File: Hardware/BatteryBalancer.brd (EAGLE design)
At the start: 93.6 x 20.1 mm, 94 parts, among them IC1 OP-AMP, J2 ISP, U1 TAP_POINT, U10 MCP1755, U11 AD7280A, U12 ATMEGA328P_TQFP, U13 CH340C, U2 TAP_POINT, U3 TAP_POINT, U4 TAP_POINT, U5 TAP_POINT, Y1 16MHz

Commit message: Panelized + cammed
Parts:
- added U$8: (no value), echoic#JPG:ECHOIC#JPG
- added U$9: (no value), tech#JPG:TECH#JPG
- moved R34 126.8 mm to (30.4, 2.67), turned to 135 degrees
- moved R10 123.6 mm to (28.3, 2.54), turned to 315 degrees
- moved C2 31.4 mm to (72.4, 2.40)
- moved C1 31.3 mm to (81.9, 2.26)
- moved C12 30.5 mm to (59.2, 16.4)
- moved C19 30.5 mm to (8.38, 3.81)
- moved C3 30.5 mm to (72.5, 6.10)
- moved C4 30.5 mm to (72.5, 9.40)
- moved C5 30.5 mm to (72.5, 12.7)
- moved C6 30.5 mm to (72.5, 16.0)
- moved D3 30.5 mm to (50.3, 3.43)
- moved D5 30.5 mm to (79.4, 19.1)
- moved D6 30.5 mm to (54.6, 19.1)
- moved D7 30.5 mm to (29.8, 19.1)
- moved J1 30.5 mm to (4.19, 6.48)
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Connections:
- net RESET renamed !RESET
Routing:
- net CHARGE: track 21.1 -> 39.7 mm, vias 3 -> 4
- net N$40: track 31.6 -> 25.6 mm
- net GND: track 24.5 -> 26.8 mm, vias 89 -> 86
- net V_RAW: track 47.1 -> 45.8 mm
- net !RESET: track 90.1 -> 89.6 mm, vias 5 -> 4
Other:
- board size 93.6 x 20.1 mm -> 93.3 x 20.3 mm

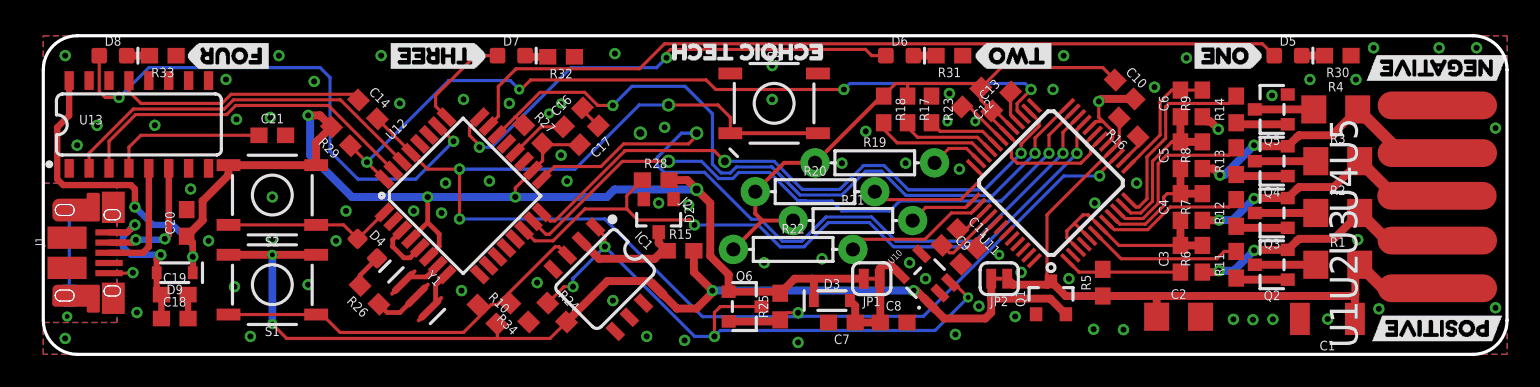
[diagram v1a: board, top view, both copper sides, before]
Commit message: Increase manufacturability, re panelize + CAM
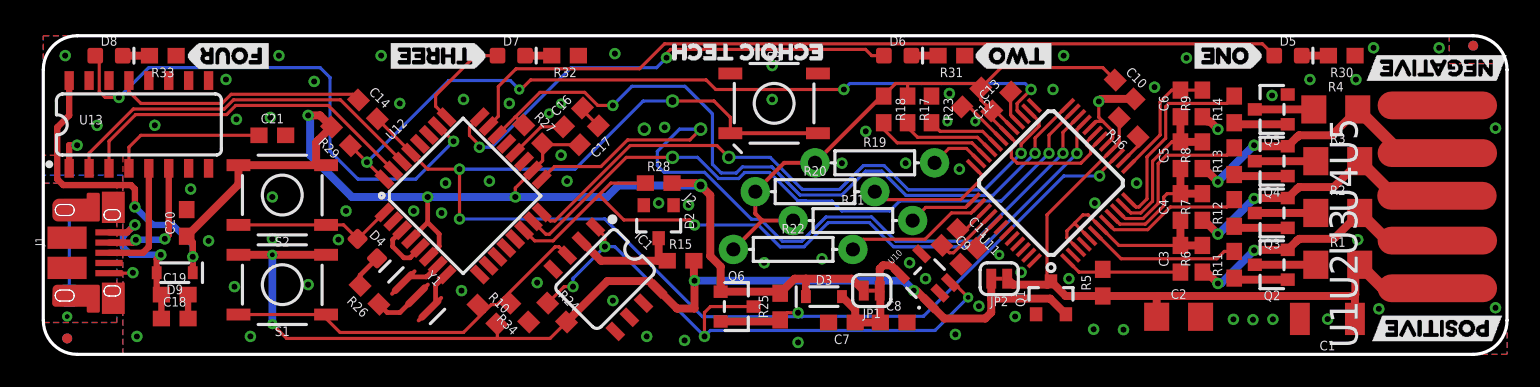
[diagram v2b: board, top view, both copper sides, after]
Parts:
- added FD1, FD2, FD3, FD4: FIDUCIALUFIDUCIAL, SparkFun-Aesthetics:FIDUCIAL-MICRO
- moved FRAME1 83.7 mm to (11.4, -12.1)
- moved JP1 0.76 mm to (52.8, 4.06)
- moved R15 0.63 mm to (40.6, 5.97)
- moved S1 0.63 mm to (15.2, 4.45)
- moved S2 0.63 mm to (15.2, 10.2)
- moved D3 0.57 mm to (49.8, 3.68)
- moved Q6 0.51 mm to (44.2, 3.05)
- moved D2 0.38 mm to (39.2, 8.51)
- moved J2 0.36 mm to (41.0, 13.5)
- moved R28 0.27 mm to (39.2, 10.9)
- moved R32 0.27 mm to (33.3, 19.1)
- moved R30 0.25 mm to (82.8, 19.1)
- moved D8 0.25 mm to (4.19, 19.0)
- moved D6 0.13 mm to (54.5, 19.1)
- moved R31 0.13 mm to (57.9, 19.1)
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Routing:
- net GND: track 26.8 -> 28.8 mm, vias 86 -> 84
- net !CS: track 45.6 -> 47.3 mm
- net VCC: track 97.6 -> 99.1 mm
- net SCLK: track 49.1 -> 49.9 mm
- net N$8: track 17.4 -> 18.2 mm
- net !RESET: track 89.6 -> 90.3 mm
- net TEST: track 11.0 -> 10.4 mm
- net N$6: track 17.3 -> 17.9 mm
